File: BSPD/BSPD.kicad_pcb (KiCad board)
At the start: 2 copper layers, 102.9 x 124.7 mm, 55 parts, among them J1 DT13-48PABCD-R015, K1 Latching Relay, Q2 STS6NF20V, Q3 STS6NF20V, U1 4081, U10 DK1A1B-12V, U11 TLP3122AE, U12 OP AMP, U13 LM7805_TO220, U14 ISO1050DUB, U15 LM7809_TO220, U2 OP AMP, U3 OP AMP, U4 NUCLEO-L432KC, U5 2x4 OR GATE, U6 LM555N, U7 TLP3122AE, U9 74LVC1GU04DRL

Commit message: more small changes
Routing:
- net Net-(U6-THR): track 21.3 -> 18.4 mm
- net /BSPD Fault: track 35.4 -> 36.3 mm
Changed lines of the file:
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@@
     (property "Sheetname" "")
     (attr through_hole)
-    (fp_text reference "U6" (at 3.8 0.625) (layer "F.SilkS")
+    (fp_text reference "U6" (at 4.181 3.038) (layer "F.SilkS")
         (effects (font (size 1 1) (thickness 0.15)))
     )
@@
     (property "ki_keywords" "cap capacitor")
     (attr smd)
-    (fp_text reference "C12" (at 2.5615 0.254 180) (layer "F.SilkS")
+    (fp_text reference "C12" (at 2.5615 1.143 180) (layer "F.SilkS")
         (effects (font (size 1 1) (thickness 0.15)))
     )
@@
     (effects (font (size 0.5 0.5) (thickness 0.075)) (justify left bottom))
   )
-  (gr_text "555\nTIMER\n" (at 106.68 75.565) (layer "F.SilkS")
+  (gr_text "555\nTIMER\n" (at 106.553 78.486) (layer "F.SilkS")
     (effects (font (size 1 1) (thickness 0.15)) (justify left bottom))
   )
@@
     (effects (font (size 0.5 0.5) (thickness 0.075)) (justify left bottom))
   )
-  (gr_text "100nf\n" (at 89.408 57.658 90) (layer "F.SilkS")
+  (gr_text "100nf\n" (at 89.408 59.055 90) (layer "F.SilkS")
     (effects (font (size 0.5 0.5) (thickness 0.075)) (justify left bottom))
   )
@@
     (effects (font (size 0.5 0.5) (thickness 0.075)) (justify left bottom))
   )
-  (gr_text "330nf\n" (at 77.724 111.125) (layer "F.SilkS")
+  (gr_text "100nf\n" (at 77.724 111.125) (layer "F.SilkS")
     (effects (font (size 0.5 0.5) (thickness 0.075)) (justify left bottom))
   )
@@
     (effects (font (size 0.5 0.5) (thickness 0.075)) (justify left bottom))
   )
-  (gr_text "100nf\n" (at 103.251 69.088 90) (layer "F.SilkS")
+  (gr_text "100nf\n" (at 103.251 70.231 90) (layer "F.SilkS")
     (effects (font (size 0.5 0.5) (thickness 0.075)) (justify left bottom))
   )
@@
   (segment (start 70.342 39.116) (end 70.342 41.275) (width 0.25) (layer "F.Cu") (net 31))
   (segment (start 76.723 39.116) (end 70.342 39.116) (width 0.25) (layer "F.Cu") (net 31))
-  (segment (start 110.1305 77.7225) (end 112.659 75.194) (width 0.25) (layer "F.Cu") (net 32))
-  (segment (start 110.119 77.734) (end 105.039 72.654) (width 0.25) (layer "F.Cu") (net 32))
-  (segment (start 112.659 75.194) (end 110.119 77.734) (width 0.25) (layer "F.Cu") (net 32))
+  (segment (start 111.252 76.454) (end 110.49 76.454) (width 0.25) (layer "F.Cu") (net 32))
+  (segment (start 111.252 76.454) (end 112.512 75.194) (width 0.25) (layer "F.Cu") (net 32))
+  (segment (start 106.69 72.654) (end 105.039 72.654) (width 0.25) (layer "F.Cu") (net 32))
+  (segment (start 110.1305 82.042) (end 111.252 80.9205) (width 0.25) (layer "F.Cu") (net 32))
+  (segment (start 112.659 75.194) (end 112.639 75.194) (width 0.25) (layer "F.Cu") (net 32))
+  (segment (start 110.49 76.454) (end 106.69 72.654) (width 0.25) (layer "F.Cu") (net 32))
   (segment (start 113.395 75.93) (end 112.659 75.194) (width 0.25) (layer "F.Cu") (net 32))
-  (segment (start 110.1305 82.042) (end 110.1305 77.7225) (width 0.25) (layer "F.Cu") (net 32))
+  (segment (start 112.512 75.194) (end 112.659 75.194) (width 0.25) (layer "F.Cu") (net 32))
+  (segment (start 111.252 80.9205) (end 111.252 76.454) (width 0.25) (layer "F.Cu") (net 32))
   (segment (start 114.935 75.93) (end 113.395 75.93) (width 0.25) (layer "F.Cu") (net 32))
   (segment (start 69.283 48.986) (end 69.283 46.518) (width 0.25) (layer "F.Cu") (net 33))
@@
   (segment (start 59.563 94.784) (end 54.13 100.217) (width 1.1) (layer "F.Cu") (net 36))
   (segment (start 59.563 91.493) (end 59.563 94.784) (width 1.1) (layer "F.Cu") (net 36))
+  (segment (start 106.553 82.042) (end 105.039 80.528) (width 0.25) (layer "F.Cu") (net 37))
   (segment (start 100.093139 51.579139) (end 98.933 50.419) (width 0.25) (layer "F.Cu") (net 37))
-  (segment (start 108.0555 82.042) (end 108.0555 80.7505) (width 0.25) (layer "F.Cu") (net 37))
-  (segment (start 108.0555 80.7505) (end 105.039 77.734) (width 0.25) (layer "F.Cu") (net 37))
+  (segment (start 108.0555 82.042) (end 106.553 82.042) (width 0.25) (layer "F.Cu") (net 37))
+  (segment (start 105.039 80.528) (end 105.039 77.734) (width 0.25) (layer "F.Cu") (net 37))
   (segment (start 100.093139 57.129639) (end 100.093139 51.579139) (width 0.25) (layer "F.Cu") (net 37))
   (segment (start 100.39239 57.42889) (end 100.093139 57.129639) (width 0.25) (layer "F.Cu") (net 37))
@@
   (segment (start 36.33 44.057) (end 51.7 59.427) (width 0.25) (layer "B.Cu") (net 50))
   (segment (start 51.7 64.273) (end 59.817 72.39) (width 0.25) (layer "B.Cu") (net 50))
-  (segment (start 70.605 51.68) (end 72.105174 51.68) (width 0.25) (layer "F.Cu") (net 52))
+  (segment (start 75.782 55.833695) (end 75.782 55.97) (width 0.25) (layer "F.Cu") (net 52))
+  (segment (start 72.517 52.091826) (end 72.517 53.594) (width 0.25) (layer "F.Cu") (net 52))
   (segment (start 75.782 55.97) (end 77.343698 57.531698) (width 0.25) (layer "F.Cu") (net 52))
-  (segment (start 74.050305 54.102) (end 75.782 55.833695) (width 0.25) (layer "F.Cu") (net 52))
-  (segment (start 77.343698 57.531698) (end 78.485302 57.531698) (width 0.25) (layer "F.Cu") (net 52))
-  (segment (start 72.517 54.102) (end 74.050305 54.102) (width 0.25) (layer "F.Cu") (net 52))
+  (segment (start 73.923305 53.975) (end 75.782 55.833695) (width 0.25) (layer "F.Cu") (net 52))
   (segment (start 85.344 61.214) (end 85.344 63.754) (width 0.25) (layer "F.Cu") (net 52))
+  (segment (start 70.605 51.68) (end 72.105174 51.68) (width 0.25) (layer "F.Cu") (net 52))
   (segment (start 78.485302 57.531698) (end 82.167604 61.214) (width 0.25) (layer "F.Cu") (net 52))
+  (segment (start 77.343698 57.531698) (end 78.485302 57.531698) (width 0.25) (layer "F.Cu") (net 52))
+  (segment (start 72.517 53.594) (end 72.898 53.975) (width 0.25) (layer "F.Cu") (net 52))
   (segment (start 72.105174 51.68) (end 72.517 52.091826) (width 0.25) (layer "F.Cu") (net 52))
-  (segment (start 82.167604 61.214) (end 85.344 61.214) (width 0.25) (layer "F.Cu") (net 52))
-  (segment (start 72.517 52.091826) (end 72.517 54.102) (width 0.25) (layer "F.Cu") (net 52))
   (segment (start 69.58 52.705) (end 70.605 51.68) (width 0.25) (layer "F.Cu") (net 52))
-  (segment (start 75.782 55.833695) (end 75.782 55.97) (width 0.25) (layer "F.Cu") (net 52))
+  (segment (start 82.167604 61.214) (end 85.344 61.214) (width 0.25) (layer "F.Cu") (net 52))
+  (segment (start 72.898 53.975) (end 73.923305 53.975) (width 0.25) (layer "F.Cu") (net 52))
   (segment (start 59.817 102.1455) (end 58.5845 103.378) (width 0.25) (layer "F.Cu") (net 53))
   (segment (start 58.5845 103.378) (end 48.391 103.378) (width 0.25) (layer "F.Cu") (net 53))

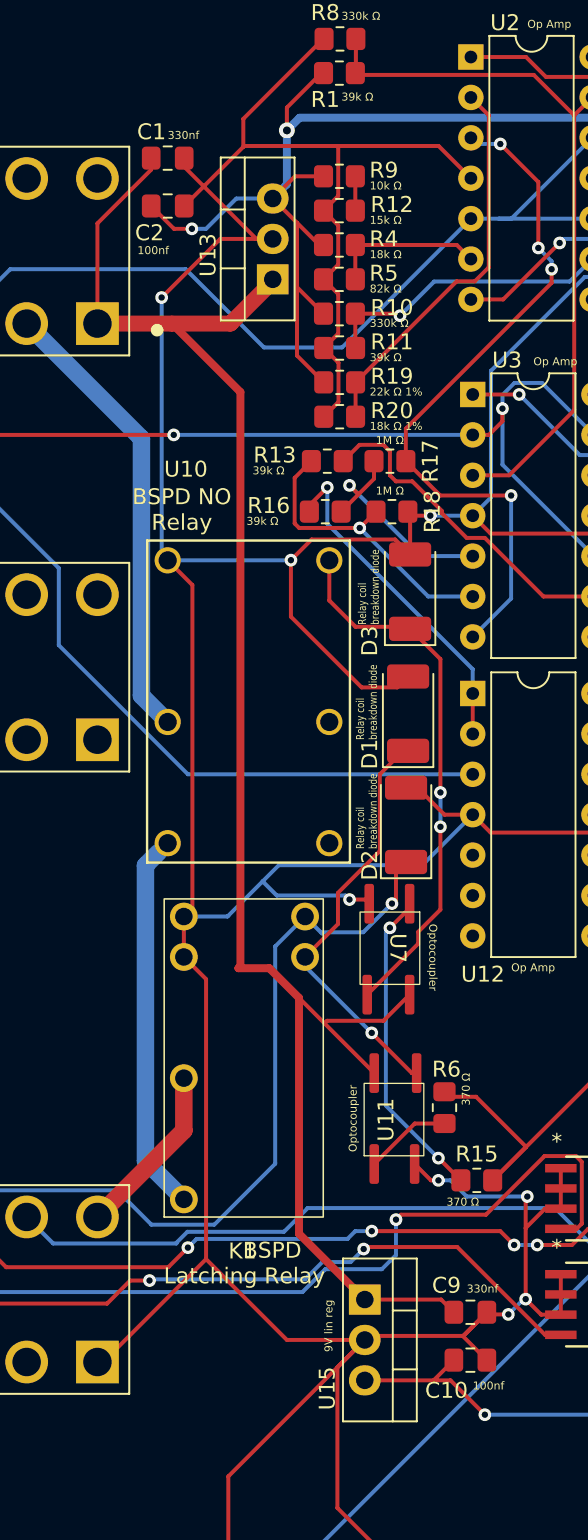
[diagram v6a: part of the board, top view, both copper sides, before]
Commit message: more trace and silkscreen fixes
(sharp angles and overlapping)
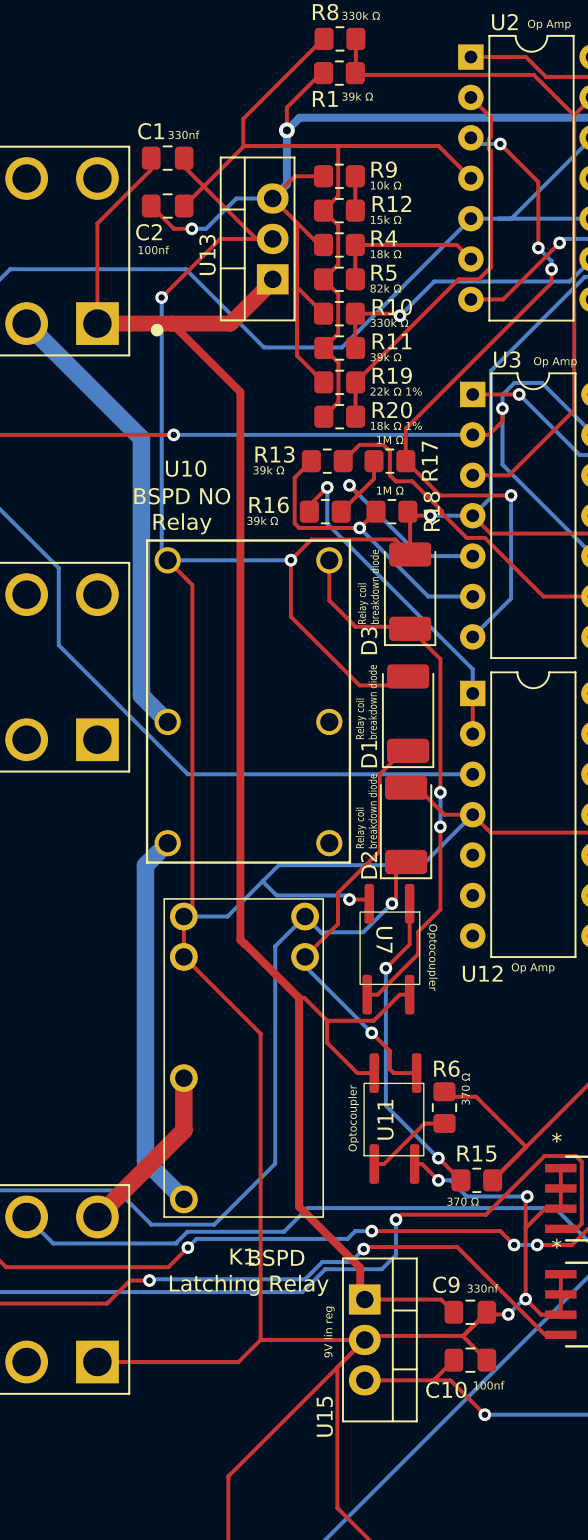
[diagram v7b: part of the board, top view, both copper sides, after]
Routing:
- net GND: track 484.7 -> 486.8 mm
- net Net-(D1-K): track 26.2 -> 26.8 mm
- net +12V: track 110.4 -> 109.8 mm
